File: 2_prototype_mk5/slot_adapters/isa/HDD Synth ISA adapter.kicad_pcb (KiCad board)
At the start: 2 copper layers, 119.4 x 97.4 mm, 16 parts, among them J1 Conn_01x02_Socket, J2 Conn_01x05_Socket, J3 Bus_ISA_8bit, J4 Conn_01x02_Socket, SW1 SW_Push, SW2 PEC12R-2120F-S0012

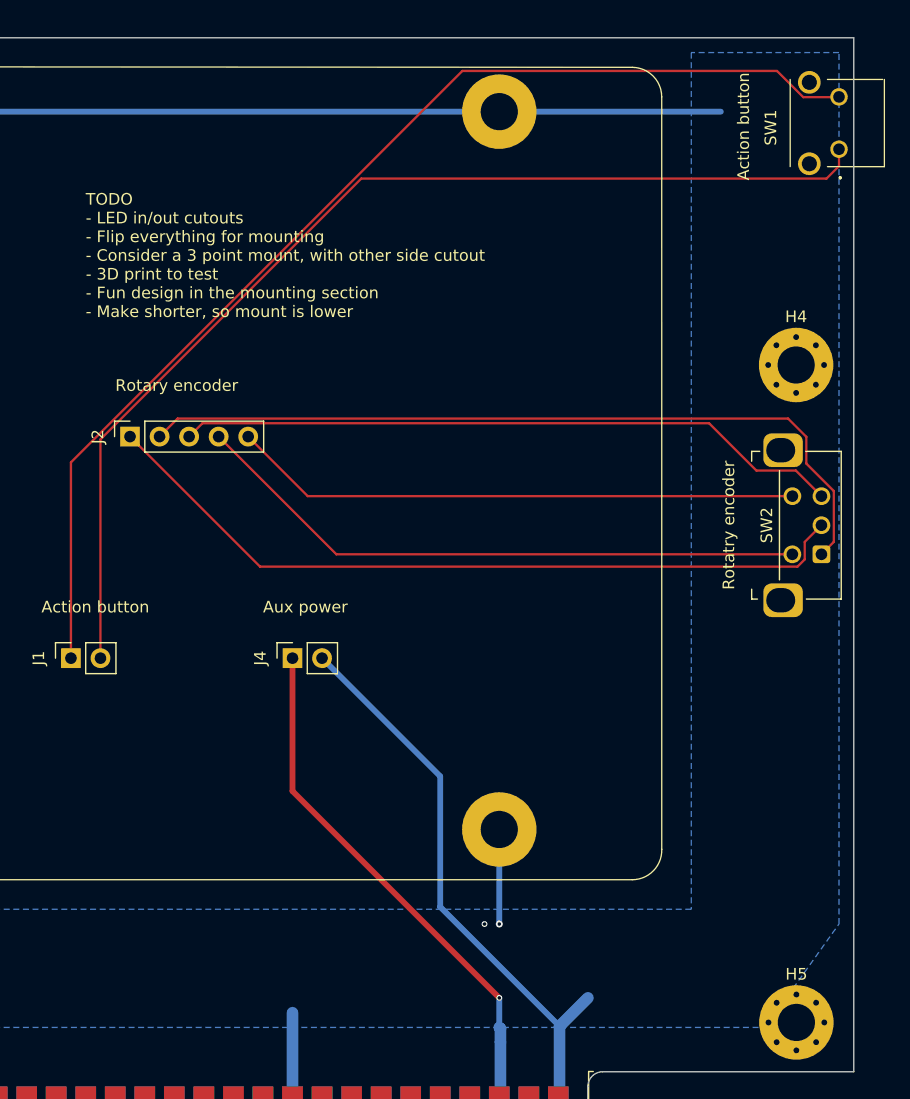
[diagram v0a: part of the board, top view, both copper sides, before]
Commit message: Cost reductions for JCLPCB
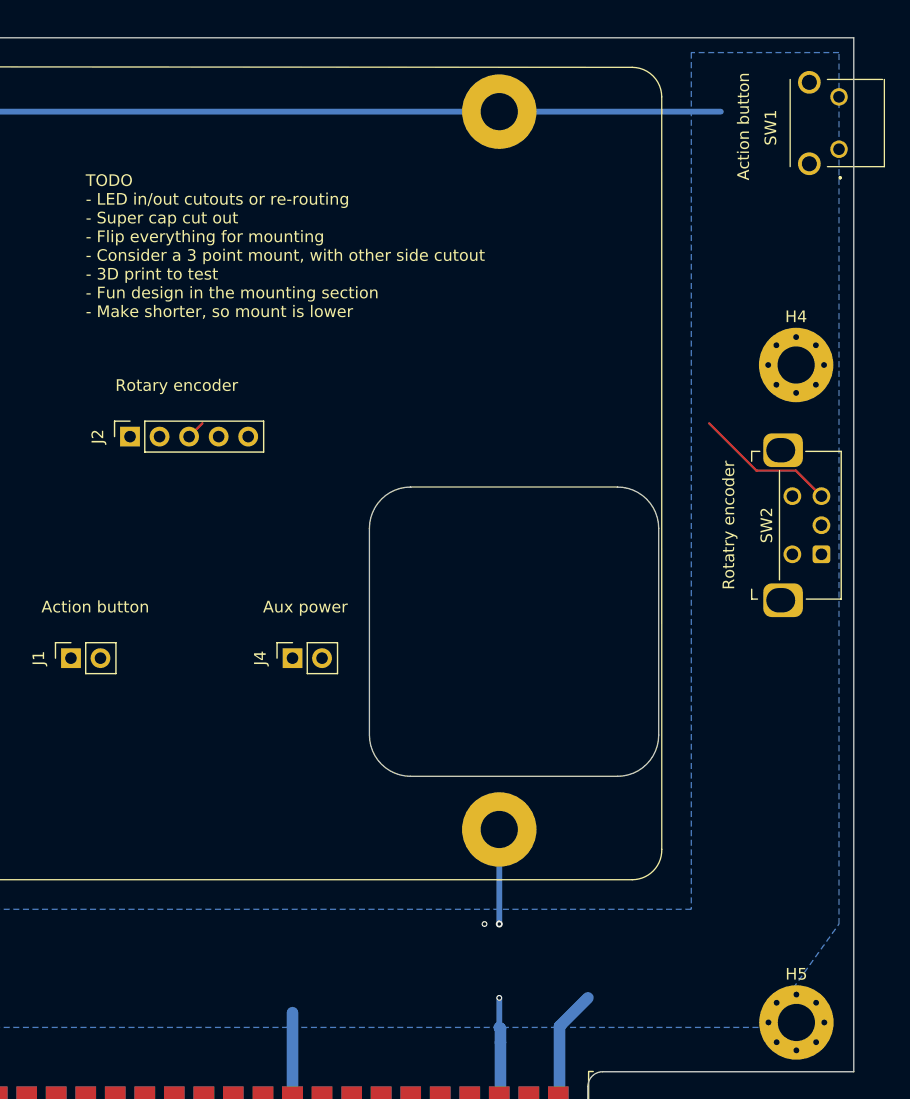
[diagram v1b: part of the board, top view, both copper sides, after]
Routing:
- net Net-(J1-Pin_1): track 97.8 -> 0.00 mm
- net Net-(J1-Pin_2): track 93.5 -> 0.00 mm
- net /ENC_A: track 68.4 -> 0.00 mm
- net Net-(J2-Pin_1): track 66.4 -> 0.00 mm
- net /ENC_SWITCH: track 53.5 -> 0.00 mm
- net Net-(J2-Pin_5): track 48.9 -> 0.00 mm
- net /ENC_B: track 57.4 -> 13.9 mm
- net GND: track 168.4 -> 128.2 mm
- net Net-(J4-Pin_1): track 48.9 -> 12.3 mm
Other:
- outline, holes or cut-outs redrawn
- board text added: "TODO - LED in/out cutouts or re-routing - Super cap cut out - Flip everything for mounting - Consider a 3 point mount, with other side cutout - 3D print to test - Fun design in the mounting section - Make shorter, so mount is lower"
- board text removed: "TODO - LED in/out cutouts - Flip everything for mounting - Consider a 3 point mount, with other side cutout - 3D print to test - Fun design in the mounting section - Make shorter, so mount is lower"
